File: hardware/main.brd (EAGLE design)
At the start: 87.6 x 56.6 mm, 49 parts, among them U1 SN74LVC4245A_DW_24, U5 SN74LVC4245A_DW_24, U9 LM3940SOT223

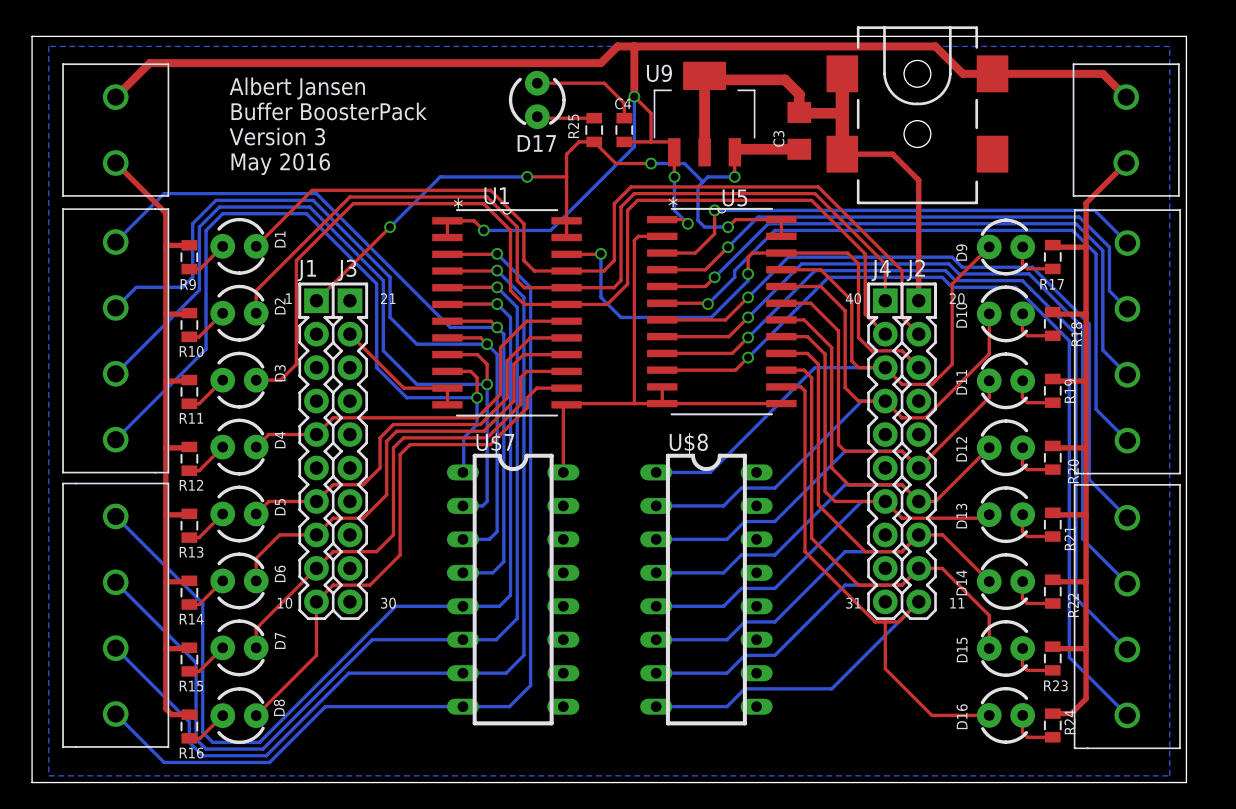
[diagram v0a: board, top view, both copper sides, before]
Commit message: Updated with DRC modifications
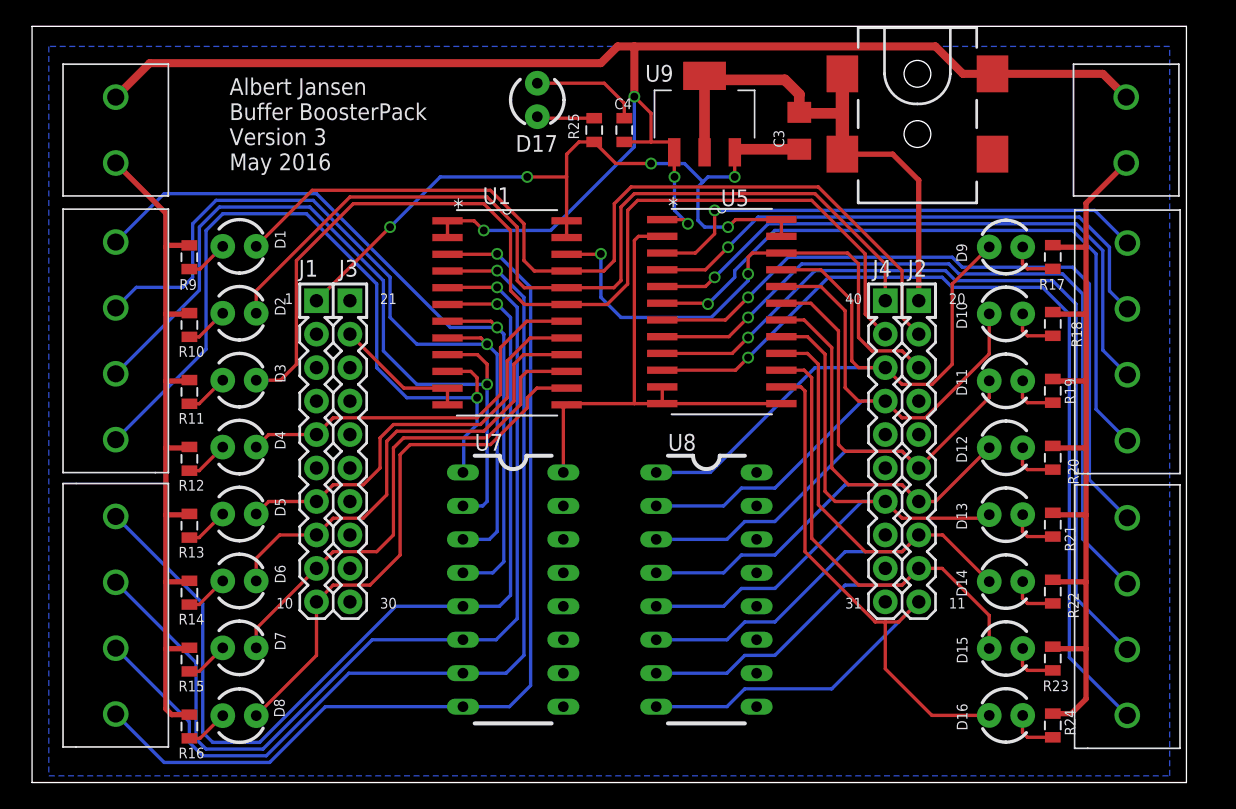
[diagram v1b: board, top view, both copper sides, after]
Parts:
- renumbered U$7 to U7, U$8 to U8
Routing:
- net N$21: track 52.4 -> 54.2 mm
- net N$22: track 57.1 -> 58.5 mm
- net N$23: track 61.6 -> 62.9 mm
- net N$24: track 66.1 -> 67.3 mm
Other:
- board size 87.6 x 56.6 mm -> 87.6 x 57.4 mm

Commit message: Minor component value changes. Added a BOM
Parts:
- R17, R18, R19, R20, R21, R22, R23, R24: value 300 -> 330
- R25: value 4.7k -> 330
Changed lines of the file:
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@@
 <attribute name="VALUE" x="48.9056" y="26.225" size="1.27" layer="27" ratio="6" rot="SR0"/>
 </element>
-<element name="R17" library="SparkFun-Resistors" package="0805" value="300" x="77.486" y="39.894" smashed="yes" rot="R90">
+<element name="R17" library="SparkFun-Resistors" package="0805" value="330" x="77.486" y="39.894" smashed="yes" rot="R90">
 <attribute name="NAME" x="76.438" y="37.4175" size="0.8128" layer="25" font="vector"/>
 <attribute name="VALUE" x="78.883" y="38.878" size="0.4064" layer="27" rot="R90"/>
@@
 <attribute name="VALUE" x="75.835" y="3.445" size="1.27" layer="27" ratio="10"/>
 </element>
-<element name="R18" library="SparkFun-Resistors" package="0805" value="300" x="77.486" y="34.814" smashed="yes" rot="R90">
+<element name="R18" library="SparkFun-Resistors" package="0805" value="330" x="77.486" y="34.814" smashed="yes" rot="R90">
 <attribute name="NAME" x="79.7085" y="33.036" size="0.8128" layer="25" font="vector" rot="R90"/>
 <attribute name="VALUE" x="78.883" y="33.798" size="0.4064" layer="27" rot="R90"/>
 </element>
-<element name="R19" library="SparkFun-Resistors" package="0805" value="300" x="77.486" y="29.734" smashed="yes" rot="R90">
+<element name="R19" library="SparkFun-Resistors" package="0805" value="330" x="77.486" y="29.734" smashed="yes" rot="R90">
 <attribute name="NAME" x="79.2005" y="28.718" size="0.8128" layer="25" font="vector" rot="R90"/>
 <attribute name="VALUE" x="78.883" y="28.718" size="0.4064" layer="27" rot="R90"/>
 </element>
-<element name="R20" library="SparkFun-Resistors" package="0805" value="300" x="77.486" y="24.654" smashed="yes" rot="R90">
+<element name="R20" library="SparkFun-Resistors" package="0805" value="330" x="77.486" y="24.654" smashed="yes" rot="R90">
 <attribute name="NAME" x="79.4545" y="22.622" size="0.8128" layer="25" font="vector" rot="R90"/>
 <attribute name="VALUE" x="78.883" y="23.638" size="0.4064" layer="27" rot="R90"/>
 </element>
-<element name="R21" library="SparkFun-Resistors" package="0805" value="300" x="77.486" y="19.574" smashed="yes" rot="R90">
+<element name="R21" library="SparkFun-Resistors" package="0805" value="330" x="77.486" y="19.574" smashed="yes" rot="R90">
 <attribute name="NAME" x="79.2005" y="17.542" size="0.8128" layer="25" font="vector" rot="R90"/>
 <attribute name="VALUE" x="78.883" y="18.558" size="0.4064" layer="27" rot="R90"/>
 </element>
-<element name="R22" library="SparkFun-Resistors" package="0805" value="300" x="77.486" y="14.494" smashed="yes" rot="R90">
+<element name="R22" library="SparkFun-Resistors" package="0805" value="330" x="77.486" y="14.494" smashed="yes" rot="R90">
 <attribute name="NAME" x="79.4545" y="12.462" size="0.8128" layer="25" font="vector" rot="R90"/>
 <attribute name="VALUE" x="78.883" y="13.478" size="0.4064" layer="27" rot="R90"/>
 </element>
-<element name="R23" library="SparkFun-Resistors" package="0805" value="300" x="77.486" y="9.414" smashed="yes" rot="R90">
+<element name="R23" library="SparkFun-Resistors" package="0805" value="330" x="77.486" y="9.414" smashed="yes" rot="R90">
 <attribute name="NAME" x="76.724" y="6.9375" size="0.8128" layer="25" font="vector"/>
 <attribute name="VALUE" x="78.883" y="8.398" size="0.4064" layer="27" rot="R90"/>
 </element>
-<element name="R24" library="SparkFun-Resistors" package="0805" value="300" x="77.486" y="4.334" smashed="yes" rot="R90">
+<element name="R24" library="SparkFun-Resistors" package="0805" value="330" x="77.486" y="4.334" smashed="yes" rot="R90">
 <attribute name="NAME" x="79.2005" y="3.572" size="0.8128" layer="25" font="vector" rot="R90"/>
 <attribute name="VALUE" x="78.883" y="3.318" size="0.4064" layer="27" rot="R90"/>
@@
 <attribute name="VALUE" x="40.005" y="53.721" size="1.27" layer="27" ratio="10" rot="R90"/>
 </element>
-<element name="R25" library="SparkFun-Resistors" package="0805" value="4.7k" x="42.672" y="49.53" smashed="yes" rot="R90">
+<element name="R25" library="SparkFun-Resistors" package="0805" value="330" x="42.672" y="49.53" smashed="yes" rot="R90">
 <attribute name="NAME" x="40.7035" y="50.8" size="0.8128" layer="25" font="vector" rot="R270"/>
 <attribute name="VALUE" x="44.069" y="48.514" size="0.4064" layer="27" rot="R90"/>

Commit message: Removed 'ENEXT', as it is not needed
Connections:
- removed net ENEXT: A1.36
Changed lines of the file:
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@@
 <wire x1="60.706" y1="7.112" x2="67.31" y2="13.716" width="0.254" layer="16"/>
-</signal>
-<signal name="ENEXT">
-<contactref element="A1" pad="36"/>
 </signal>
 <signal name="N$33">

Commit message: Added helpful silkscreen markings
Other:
- board size 87.6 x 57.4 mm -> 89.4 x 57.4 mm
- board text added: "+"
- board text added: "-"
- board text added: "1"
- board text added: "2"
- board text added: "3"
- board text added: "4"
- board text added: "5"
- board text added: "6"
- board text added: "7"
- board text added: "8"
- board text added: "INPUT"
- board text added: "OUTPUT"
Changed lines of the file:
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@@
 <board>
 <plain>
-<wire x1="0" y1="0" x2="87.63" y2="0" width="0" layer="20"/>
-<wire x1="87.63" y1="0" x2="87.63" y2="57.404" width="0" layer="20"/>
-<wire x1="87.63" y1="57.404" x2="0" y2="57.404" width="0" layer="20"/>
+<wire x1="0" y1="0" x2="89.408" y2="0" width="0" layer="20"/>
+<wire x1="89.408" y1="0" x2="89.408" y2="57.15" width="0" layer="20"/>
+<wire x1="89.408" y1="57.15" x2="0" y2="57.404" width="0" layer="20"/>
 <wire x1="0" y1="57.404" x2="0" y2="0" width="0" layer="20"/>
 <text x="14.986" y="46.482" size="1.27" layer="25" font="vector">Albert Jansen
@@
 Version 3
 May 2016</text>
+<text x="2.032" y="41.91" size="1.27" layer="21" font="vector" rot="R180">1</text>
+<text x="1.778" y="36.83" size="1.27" layer="21" font="vector" rot="R180">2</text>
+<text x="1.778" y="31.75" size="1.27" layer="21" font="vector" rot="R180">3</text>
+<text x="1.778" y="26.67" size="1.27" layer="21" font="vector" rot="R180">4</text>
+<text x="1.778" y="20.828" size="1.27" layer="21" font="vector" rot="R180">5</text>
+<text x="1.778" y="15.748" size="1.27" layer="21" font="vector" rot="R180">6</text>
+<text x="1.778" y="10.668" size="1.27" layer="21" font="vector" rot="R180">7</text>
+<text x="1.778" y="5.588" size="1.27" layer="21" font="vector" rot="R180">8</text>
+<text x="89.154" y="41.91" size="1.27" layer="21" font="vector" rot="R180">1</text>
+<text x="88.9" y="36.83" size="1.27" layer="21" font="vector" rot="R180">2</text>
+<text x="88.9" y="31.75" size="1.27" layer="21" font="vector" rot="R180">3</text>
+<text x="88.9" y="26.67" size="1.27" layer="21" font="vector" rot="R180">4</text>
+<text x="88.9" y="20.828" size="1.27" layer="21" font="vector" rot="R180">5</text>
+<text x="88.9" y="15.748" size="1.27" layer="21" font="vector" rot="R180">6</text>
+<text x="88.9" y="10.668" size="1.27" layer="21" font="vector" rot="R180">7</text>
+<text x="88.9" y="5.588" size="1.27" layer="21" font="vector" rot="R180">8</text>
+<text x="3.556" y="0.762" size="1.27" layer="21" font="vector">INPUT</text>
+<text x="80.01" y="0.762" size="1.27" layer="21" font="vector">OUTPUT</text>
+<text x="2.286" y="53.086" size="1.778" layer="21" font="vector" rot="R180">+</text>
+<text x="2.286" y="48.006" size="1.778" layer="21" font="vector" rot="R180">-</text>
+<text x="89.154" y="53.086" size="1.778" layer="21" font="vector" rot="R180">+</text>
+<text x="89.154" y="48.006" size="1.778" layer="21" font="vector" rot="R180">-</text>
 </plain>
 <attributes>
@@
 <vertex x="1.27" y="55.88"/>
 <vertex x="1.27" y="0.508"/>
-<vertex x="86.36" y="0.508"/>
-<vertex x="86.36" y="55.88"/>
+<vertex x="87.63" y="0.508"/>
+<vertex x="87.63" y="55.88"/>
 </polygon>
 <wire x1="6.35" y1="47.03" x2="10.16" y2="43.22" width="0.4064" layer="1"/>

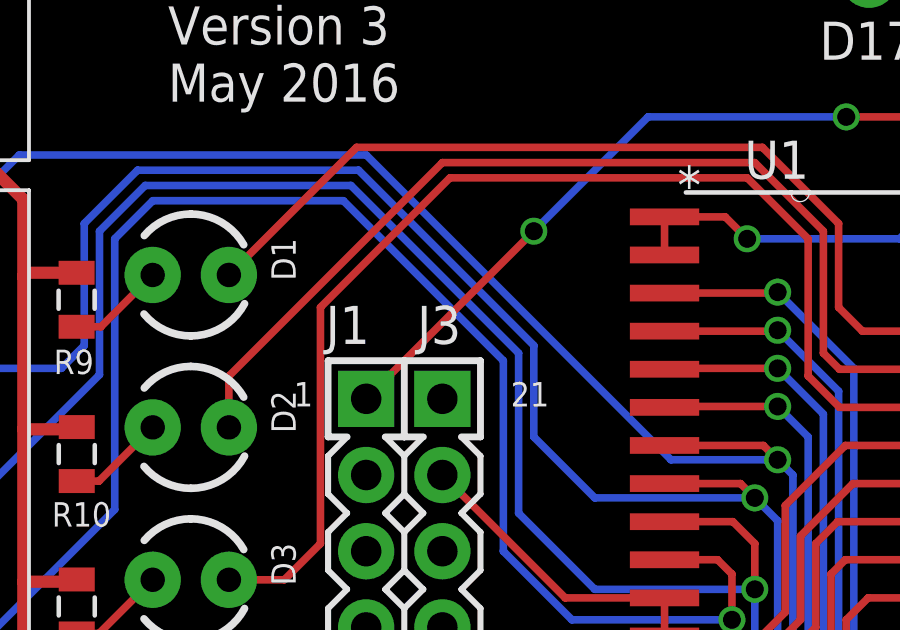
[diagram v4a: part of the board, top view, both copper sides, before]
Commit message: Small power routing update (Power the target launchpad via 3.3V connection)
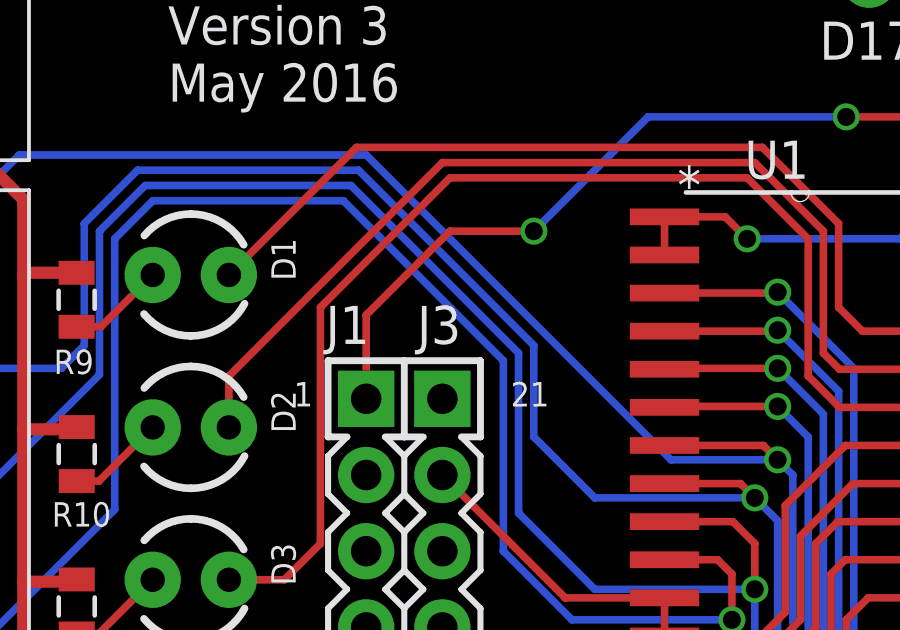
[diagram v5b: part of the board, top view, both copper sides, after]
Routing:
- net 3.3V: track 61.8 -> 63.4 mm
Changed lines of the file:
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@@
 <wire x1="53.34" y1="45.974" x2="53.34" y2="47.834" width="0.254" layer="1"/>
 <wire x1="53.34" y1="47.834" x2="53.35" y2="47.844" width="0.254" layer="1"/>
-<wire x1="21.59" y1="36.576" x2="27.178" y2="42.164" width="0.254" layer="1"/>
 <via x="27.178" y="42.164" extent="1-16" drill="0.6"/>
 <wire x1="27.178" y1="42.164" x2="30.988" y2="45.974" width="0.254" layer="16"/>
@@
 <wire x1="53.35" y1="47.844" x2="53.58" y2="48.074" width="0.8128" layer="1"/>
 <wire x1="53.58" y1="48.074" x2="58.242" y2="48.074" width="0.8128" layer="1"/>
+<wire x1="27.178" y1="42.164" x2="24.384" y2="42.164" width="0.254" layer="1"/>
+<wire x1="24.384" y1="42.164" x2="21.59" y2="39.37" width="0.254" layer="1"/>
+<wire x1="21.59" y1="39.37" x2="21.59" y2="36.576" width="0.254" layer="1"/>
 </signal>
 <signal name="5V">

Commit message: Finalized documentation and added open source licensing and logos
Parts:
- added U$7: (no value), SparkFun-Aesthetics:OSHW-LOGO-M
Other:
- outline, holes or cut-outs redrawn
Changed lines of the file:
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@@
 <plain>
 <wire x1="0" y1="0" x2="89.408" y2="0" width="0" layer="20"/>
-<wire x1="89.408" y1="0" x2="89.408" y2="57.15" width="0" layer="20"/>
-<wire x1="89.408" y1="57.15" x2="0" y2="57.404" width="0" layer="20"/>
+<wire x1="89.408" y1="0" x2="89.408" y2="57.404" width="0" layer="20"/>
+<wire x1="89.408" y1="57.404" x2="0" y2="57.404" width="0" layer="20"/>
 <wire x1="0" y1="57.404" x2="0" y2="0" width="0" layer="20"/>
 <text x="14.986" y="46.482" size="1.27" layer="25" font="vector">Albert Jansen
@@
 <attribute name="VALUE" x="50.555" y="22.143" size="1.27" layer="27" ratio="10" rot="R270"/>
 </element>
+<element name="U$7" library="SparkFun-Aesthetics" package="OSHW-LOGO-M" value="" x="29.21" y="46.99"/>
 </elements>
 <signals>
